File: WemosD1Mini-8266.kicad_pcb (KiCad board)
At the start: 2 copper layers, 79.9 x 51.8 mm, 54 parts, among them J1 Conn_01x02_Pin, J2 Screw_Terminal_01x10, J3 Conn_01x02_Pin, U1 PC817, U2 PC817, U3 PC817, U4 PC817, U5 WeMos_D1_mini, U6 ULN2003

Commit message: Version 1.1
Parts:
- removed IJ1, IJ2, IJ3, IJ4, NCI1, NCI2, NCI3, NCR1, NCR2, NCR3, RJ1, RJ2, RJ3, RJ4: TestPoint, TestPoint:TestPoint_Pad_D1.0mm
- added H1: MountingHole, MountingHole:MountingHole_3.2mm_M3, F.Cu at (170.7, 137.5)
- added J4: Conn_01x04_Pin, Connector_JST:JST_XH_B4B-XH-A_1x04_P2.50mm_Vertical, F.Cu at (156.1, 123.3)
- added J5: Conn_01x02_Pin, Connector_JST:JST_XH_B2B-XH-A_1x02_P2.50mm_Vertical, F.Cu at (182.6, 113.4)
- added J6: Conn_01x02_Pin, Connector_JST:JST_XH_B2B-XH-A_1x02_P2.50mm_Vertical, F.Cu at (174.4, 104.1)
- added J7: Conn_01x02_Pin, Connector_JST:JST_XH_B2B-XH-A_1x02_P2.50mm_Vertical, F.Cu at (183.6, 104.1)
- added J8: Screw_Terminal_01x08, TerminalBlock_Phoenix:TerminalBlock_Phoenix_MKDS-3-8-5.08_1x08_P5.08mm_Horizontal, F.Cu at (193.1, 144.7)
- added R17: 480, Resistor_SMD:R_0805_2012Metric_Pad1.20x1.40mm_HandSolder, B.Cu at (161.7, 112.9)
- added R18: 480, Resistor_SMD:R_0805_2012Metric_Pad1.20x1.40mm_HandSolder, B.Cu at (161.7, 115.3)
- added R19: 10K, Resistor_SMD:R_0805_2012Metric_Pad1.20x1.40mm_HandSolder, F.Cu at (171.7, 112.7)
- added R20: 6.8K, Resistor_SMD:R_0805_2012Metric_Pad1.20x1.40mm_HandSolder, F.Cu at (176.0, 112.7)
- added R21: 2.2K, Resistor_SMD:R_0805_2012Metric_Pad1.20x1.40mm_HandSolder, F.Cu at (171.7, 109.1)
- added R22: 5.6K, Resistor_SMD:R_0805_2012Metric_Pad1.20x1.40mm_HandSolder, F.Cu at (176.0, 109.1)
- added R23: 0, Resistor_SMD:R_0805_2012Metric_Pad1.20x1.40mm_HandSolder, F.Cu at (117.8, 138.0)
- added RV1: Varistor, Varistor:RV_Disc_D12mm_W7.1mm_P7.5mm, F.Cu at (117.8, 141.6)
- D4: moved to F.Cu
- J1: value Conn_01x02_Pin -> Screw_Terminal_01x10; footprint Connector_PinHeader_2.54mm:PinHeader_1x02_P2.54mm_Vertical -> TerminalBlock_Phoenix:TerminalBlock_Phoenix_MKDS-3-10-5.08_1x10_P5.08mm_Horizontal
- J2: value Screw_Terminal_01x10 -> Conn_01x02_Pin; footprint TerminalBlock_Phoenix:TerminalBlock_Phoenix_MKDS-3-10-5.08_1x10_P5.08mm_Horizontal -> Connector_JST:JST_XH_B2B-XH-A_1x02_P2.50mm_Vertical
- J3: footprint Connector_PinHeader_2.54mm:PinHeader_1x02_P2.54mm_Vertical -> Connector_JST:JST_XH_B2B-XH-A_1x02_P2.50mm_Vertical
- R10, R11: value 180K -> 22K; footprint Resistor_SMD:R_0805_2012Metric_Pad1.20x1.40mm_HandSolder -> Resistor_SMD:R_1206_3216Metric_Pad1.30x1.75mm_HandSolder; moved to F.Cu
- R12: value 10K -> 22K; footprint Resistor_SMD:R_0603_1608Metric_Pad0.98x0.95mm_HandSolder -> Resistor_SMD:R_1206_3216Metric_Pad1.30x1.75mm_HandSolder; moved to F.Cu
- R13: value 480 -> 22K; footprint Resistor_SMD:R_0805_2012Metric_Pad1.20x1.40mm_HandSolder -> Resistor_SMD:R_1206_3216Metric_Pad1.30x1.75mm_HandSolder
- R14: value 480 -> 10K; footprint Resistor_SMD:R_0805_2012Metric_Pad1.20x1.40mm_HandSolder -> Resistor_SMD:R_0603_1608Metric_Pad0.98x0.95mm_HandSolder; moved to B.Cu
- R15, R16: moved to B.Cu
- U1, U2, U3, U4: footprint Package_DIP:DIP-4_W7.62mm_SMDSocket_SmallPads -> Package_DIP:DIP-4_W8.89mm_SMDSocket_LongPads
- moved J2 98.0 mm to (151.6, 104.2), turned to 180 degrees
- moved C1 86.0 mm to (181.1, 121.5)
- moved C2 79.0 mm to (166.2, 127.0), turned to -90 degrees
- moved R14 78.6 mm to (147.4, 131.1), turned to 180 degrees
- moved R13 74.0 mm to (117.4, 127.5), turned to 90 degrees
- moved R11 71.3 mm to (114.0, 132.9), turned to -90 degrees
- moved R10 70.3 mm to (114.1, 127.3)
- moved R9 69.9 mm to (147.5, 137.0)
- moved U5 69.4 mm to (184.8, 143.2)
- moved R6 69.4 mm to (147.5, 142.8)
- moved PS1 69.4 mm to (123.0, 136.6)
- moved R3 69.2 mm to (147.5, 148.9)
- moved U4 69.1 mm to (137.3, 129.8)
- moved U3 69.0 mm to (137.3, 135.6)
- moved U2 68.7 mm to (137.3, 141.6)
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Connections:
- C1 pad 1: /Voltage Sensing/+Vs -> +3.3V
- J1 pad 1: Earth -> /Load4
- J1 pad 2: +5V -> /Load3
- J2 pad 1: /Load4 -> +5V
- J2 pad 2: /Load3 -> Earth
- J3 pad 1: Earth -> +3.3V
- J3 pad 2: /Voltage Sensing/+Vs -> Earth
- PS1 pad 1: /AC/L -> /AC/L(P)
- R11 pad 2: Net-(D4-K) -> Net-(R11-Pad2)
- R12 pad 1: /Voltage Sensing/+Vs -> Net-(R11-Pad2)
- R12 pad 2: /Voltage Sensing/In4 -> Net-(R12-Pad2)
- R13 pad 1: /Relays/RL1 -> Net-(R12-Pad2)
- R13 pad 2: Net-(D5-A) -> Net-(D4-K)
- R14 pad 1: /Relays/RL2 -> +3.3V
- R14 pad 2: Net-(D6-A) -> /Voltage Sensing/In4
- R3 pad 1: /Voltage Sensing/+Vs -> +3.3V
- R6 pad 1: /Voltage Sensing/+Vs -> +3.3V
- R9 pad 1: /Voltage Sensing/+Vs -> +3.3V
- U5 pad 2: unconnected-(U5-A0-Pad2) -> Net-(U5-A0)
- U5 pad 8: /Voltage Sensing/+Vs -> +3.3V
- U6 pad 11: Net-(U6-O6) -> Net-(U6-O5)
- U6 pad 13: Net-(U6-O4) -> Net-(U6-O3)
- U6 pad 15: Net-(U6-O2) -> Net-(U6-O1)
- U6 pad 2: Net-(U6-I2) -> /Relays/RL4
- U6 pad 4: Net-(U6-I4) -> /Relays/RL3
- U6 pad 6: Net-(U6-I6) -> /Relays/RL2
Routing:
- net Earth: track 39.4 -> 167.3 mm, vias 9 -> 2
- net +3.3V: track 0.00 -> 125.7 mm, vias 0 -> 2
- net /Voltage Sensing/+Vs: track 61.1 -> 0.00 mm, vias 1 -> 0
- net Net-(U5-A0): track 0.00 -> 41.5 mm
- net +5V: track 110.7 -> 70.2 mm, vias 2 -> 0
- net /Voltage Sensing/In1: track 49.5 -> 78.3 mm, vias 1 -> 0
- net Net-(J8-Pin_1): track 0.00 -> 24.0 mm
- net Net-(J8-Pin_3): track 0.00 -> 22.6 mm
- net Net-(J8-Pin_4): track 0.00 -> 22.6 mm
- net Net-(J8-Pin_2): track 0.00 -> 22.6 mm
- net /Voltage Sensing/In2: track 23.8 -> 43.8 mm
- net /Voltage Sensing/In3: track 24.3 -> 39.9 mm, vias 1 -> 2
- net /M4: track 5.20 -> 16.2 mm, vias 0 -> 1
- net Net-(D3-K): track 14.0 -> 24.6 mm, vias 0 -> 2
- net Net-(J7-Pin_1): track 0.00 -> 10.2 mm
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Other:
- board size 79.9 x 51.8 mm -> 98 x 51.1 mm
- board text added: "- IN2 IN3 IN4"
- board text added: "-3V3+"
- board text added: "-5V+"
- board text added: "IN1 -"
- board text added: "Wemos D1 Mini 4Node Control V1.1"
- board text removed: "+"
- board text removed: "-"
- board text removed: "3V3"
- board text removed: "5V"
- board text removed: "CAUTION: High Voltage"
- board text removed: "Wemos D1 Mini 4Node Control V1.0"
- board text removed: "WemosD1 Mini 4 Node V1.0"

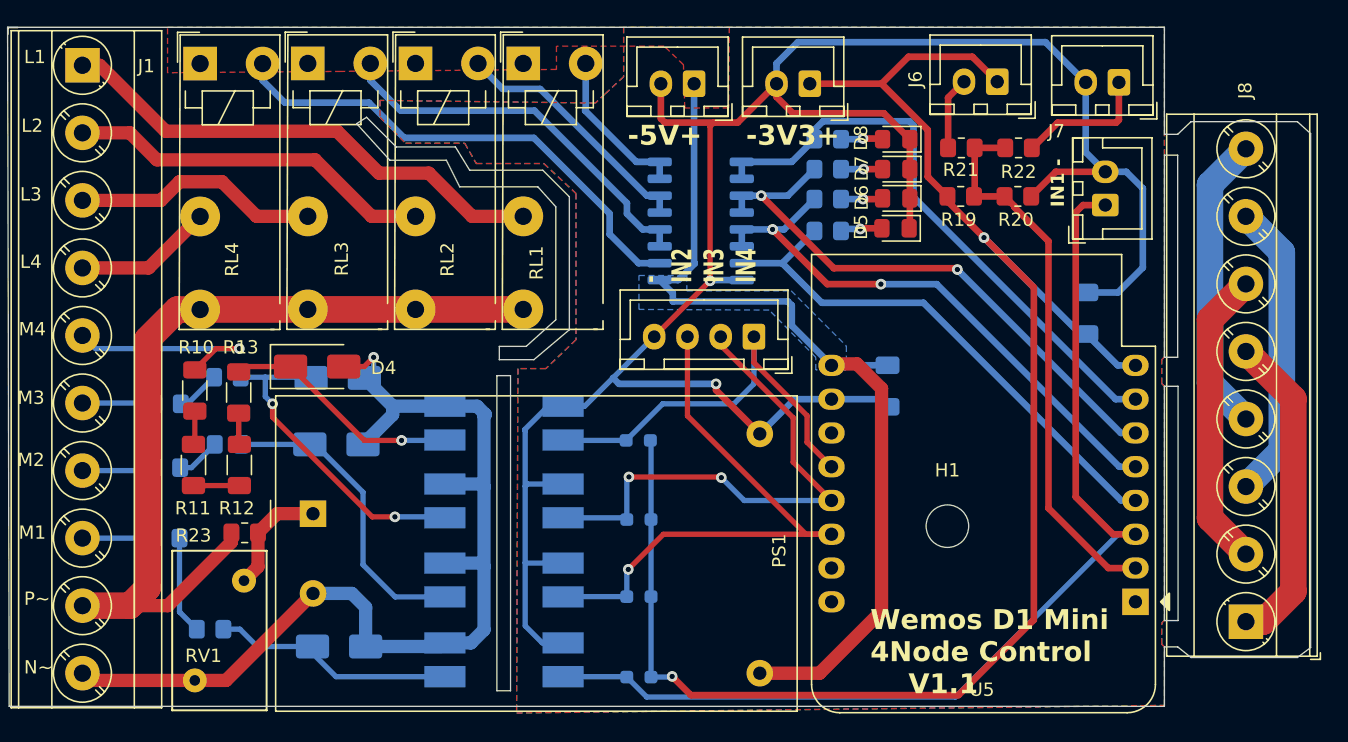
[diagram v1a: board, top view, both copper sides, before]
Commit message: Version 1.2 Updates.
Added support for 3 digital switches via ADC.  Added MOV+Fuse protection
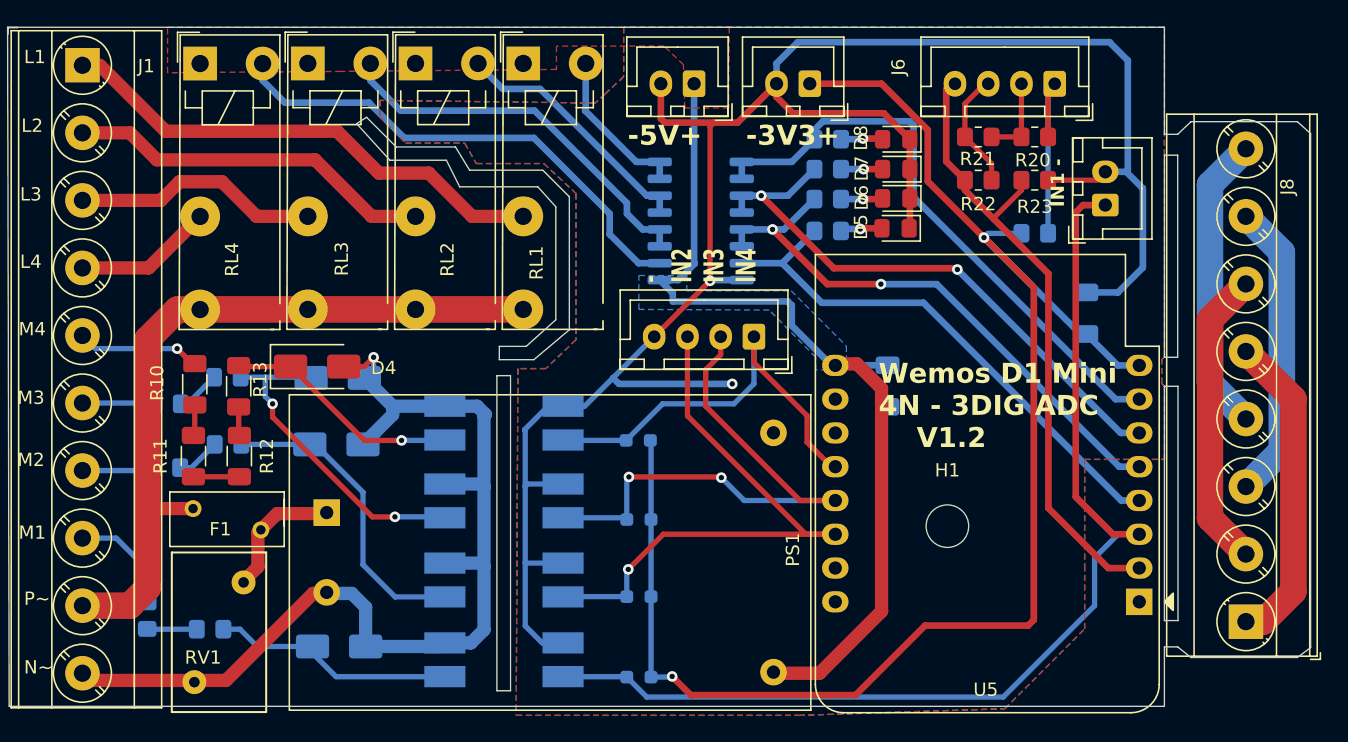
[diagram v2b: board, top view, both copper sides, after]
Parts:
- removed J7: Conn_01x02_Pin, Connector_JST:JST_XH_B2B-XH-A_1x02_P2.50mm_Vertical
- added F1: Fuse, Fuse:Fuse_BelFuse_0ZRE0005FF_L8.3mm_W3.8mm, F.Cu at (114.0, 136.2)
- J6: value Conn_01x02_Pin -> Conn_01x04_Pin; footprint Connector_JST:JST_XH_B2B-XH-A_1x02_P2.50mm_Vertical -> Connector_JST:JST_XH_B4B-XH-A_1x04_P2.50mm_Vertical
- R15: renamed from R18; value 480 -> 150
- R16: renamed from R17; value 480 -> 150
- R17: renamed from R15; value 480 -> 150
- R18: renamed from R16; value 480 -> 150
- R19: value 10K -> 470; moved to B.Cu
- R20: value 6.8K -> 470
- R21: value 2.2K -> 1K
- R22: value 5.6K -> 2.2K
- R23: value 0 -> 1.5K
- moved R23 65.1 mm to (177.2, 111.5), turned to 0 degrees
- moved R19 6.23 mm to (177.2, 115.5), turned to 180 degrees
- moved R1 6.00 mm to (110.5, 144.2), turned to -90 degrees
- moved R20 4.65 mm to (177.2, 108.2)
- moved J6 4.32 mm to (178.8, 104.2)
- moved R22 3.88 mm to (173.0, 111.5)
- moved R21 1.51 mm to (173.0, 108.2)
- moved PS1 1.03 mm to (124.0, 136.5)
- moved R11 0.67 mm to (114.0, 132.2)
- moved R12 0.67 mm to (117.4, 132.2)
- moved R10 0.47 mm to (114.1, 126.8)
- moved R13 0.47 mm to (117.4, 127.0)
- moved U5 0.29 mm to (185.1, 143.2)
- moved RV1 0.13 mm to (117.8, 141.8)
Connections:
- J6 pad 1: +3.3V -> Net-(J6-Pin_1)
- R19 pad 1: +3.3V -> Net-(J6-Pin_1)
- R19 pad 2: Net-(U5-A0) -> +3.3V
- R20 pad 1: Net-(U5-A0) -> Net-(J6-Pin_2)
- R20 pad 2: Earth -> Net-(J6-Pin_1)
- R21 pad 1: Net-(J6-Pin_2) -> Net-(J6-Pin_3)
- R21 pad 2: Net-(U5-A0) -> Net-(J6-Pin_2)
- R22 pad 1: Net-(U5-A0) -> Net-(J6-Pin_4)
- R22 pad 2: Net-(J7-Pin_1) -> Net-(J6-Pin_3)
- R23 pad 1: /AC/L(P) -> Net-(J6-Pin_4)
- R23 pad 2: /AC/L -> Earth
- U5 pad 2: Net-(U5-A0) -> Net-(J6-Pin_4)
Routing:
- net Net-(J6-Pin_4): track 0.00 -> 47.8 mm
- net Net-(U5-A0): track 41.5 -> 0.00 mm
- net Net-(J6-Pin_1): track 0.00 -> 16.2 mm
- net Earth: track 167.3 -> 154.3 mm
- net Net-(J7-Pin_1): track 10.2 -> 0.00 mm
- net Net-(J6-Pin_3): track 0.00 -> 9.05 mm
- net +3.3V: track 125.7 -> 118.4 mm
- net /AC/L: track 63.6 -> 56.8 mm
- net /M4: track 16.2 -> 9.41 mm
- net Net-(R1-Pad2): track 7.39 -> 3.74 mm
- net /M1: track 5.30 -> 8.34 mm
- net /Voltage Sensing/In3: track 39.9 -> 42.2 mm
- net /Voltage Sensing/In1: track 78.3 -> 80.4 mm
- net Net-(J6-Pin_2): track 5.47 -> 6.50 mm
- net +5V: track 70.2 -> 69.2 mm
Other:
- board text added: "S1[ S2[ S3["
- board text added: "Wemos D1 Mini 4N - 3DIG ADC V1.2"
- board text removed: "Wemos D1 Mini 4Node Control V1.1"

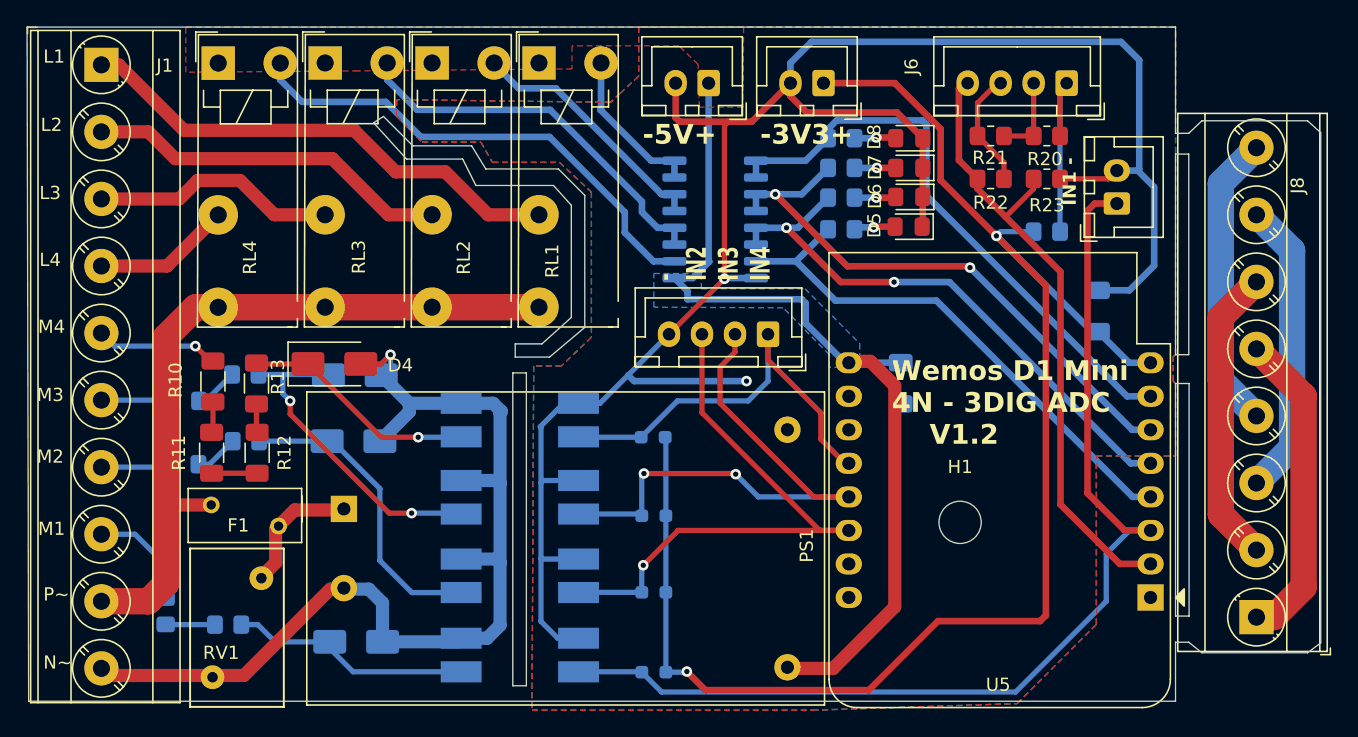
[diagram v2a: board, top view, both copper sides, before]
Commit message: V1.3 - Removed bypass PCB due to single design mandate from manufacturing.
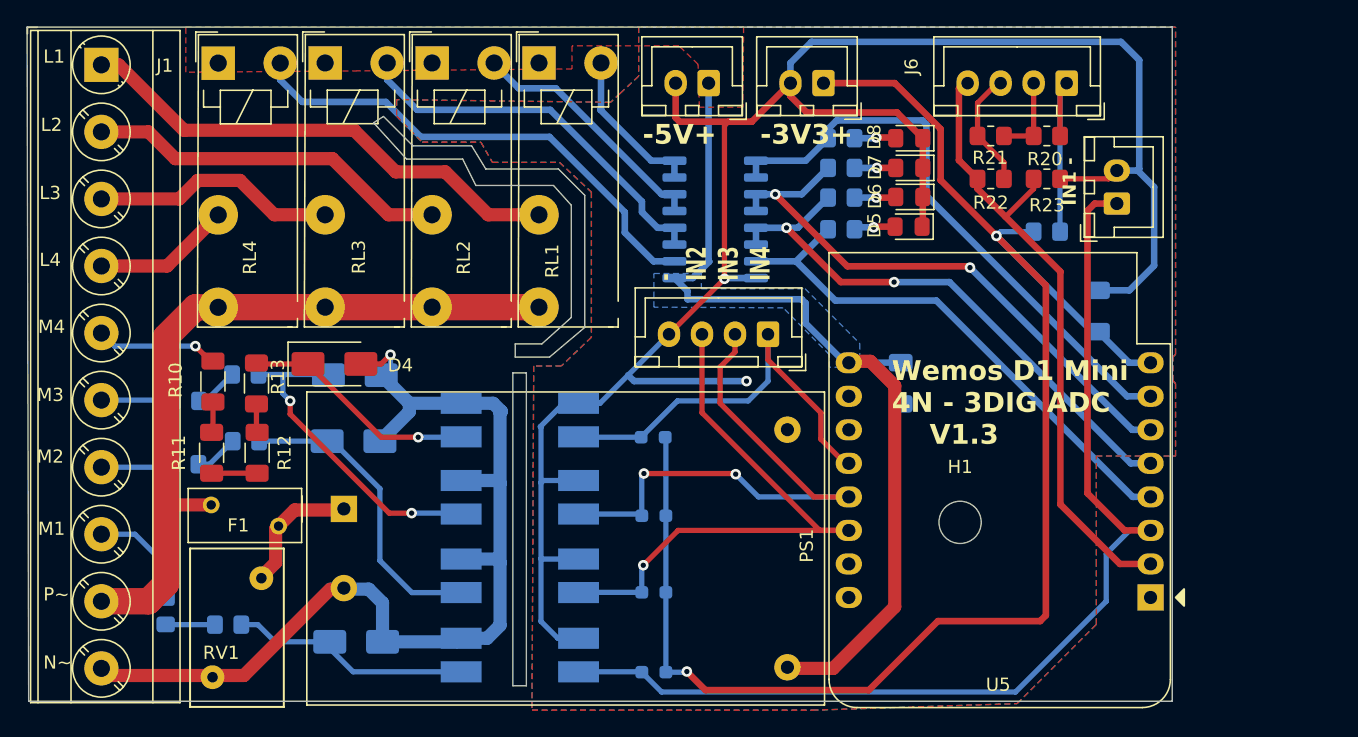
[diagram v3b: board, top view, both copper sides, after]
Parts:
- removed J8: Screw_Terminal_01x08, TerminalBlock_Phoenix:TerminalBlock_Phoenix_MKDS-3-8-5.08_1x08_P5.08mm_Horizontal
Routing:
- net Net-(J8-Pin_1): track 24.0 -> 0.00 mm
- net Net-(J8-Pin_3): track 22.6 -> 0.00 mm
- net Net-(J8-Pin_4): track 22.6 -> 0.00 mm
- net Net-(J8-Pin_2): track 22.6 -> 0.00 mm
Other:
- board size 98 x 51.1 mm -> 86.8 x 51.1 mm
- board text added: "Wemos D1 Mini 4N - 3DIG ADC V1.3"
- board text removed: "Wemos D1 Mini 4N - 3DIG ADC V1.2"
